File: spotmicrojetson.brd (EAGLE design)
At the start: 31 x 66 mm, 6 parts, among them J1 I2C1, J2 I2C2, J3 I2C3, J4 I2C4

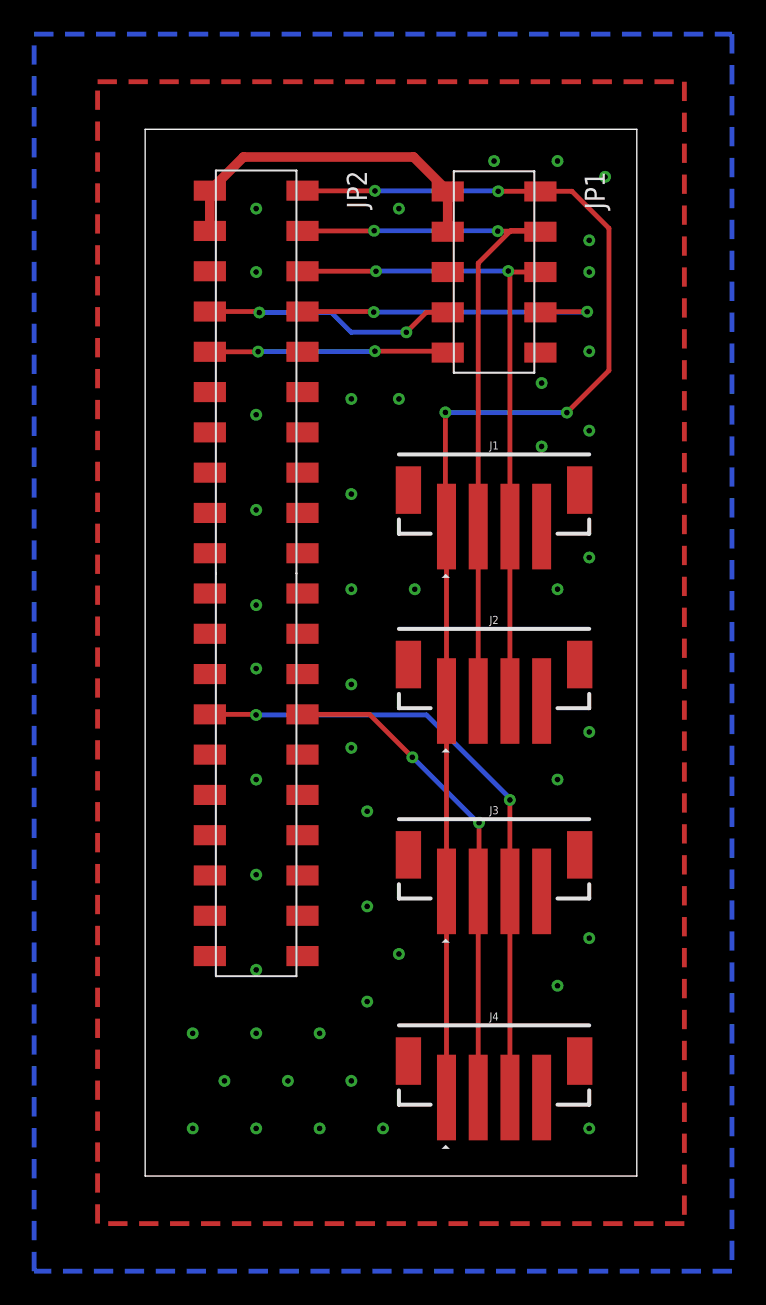
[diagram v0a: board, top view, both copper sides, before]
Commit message: Fix ground plane polygons
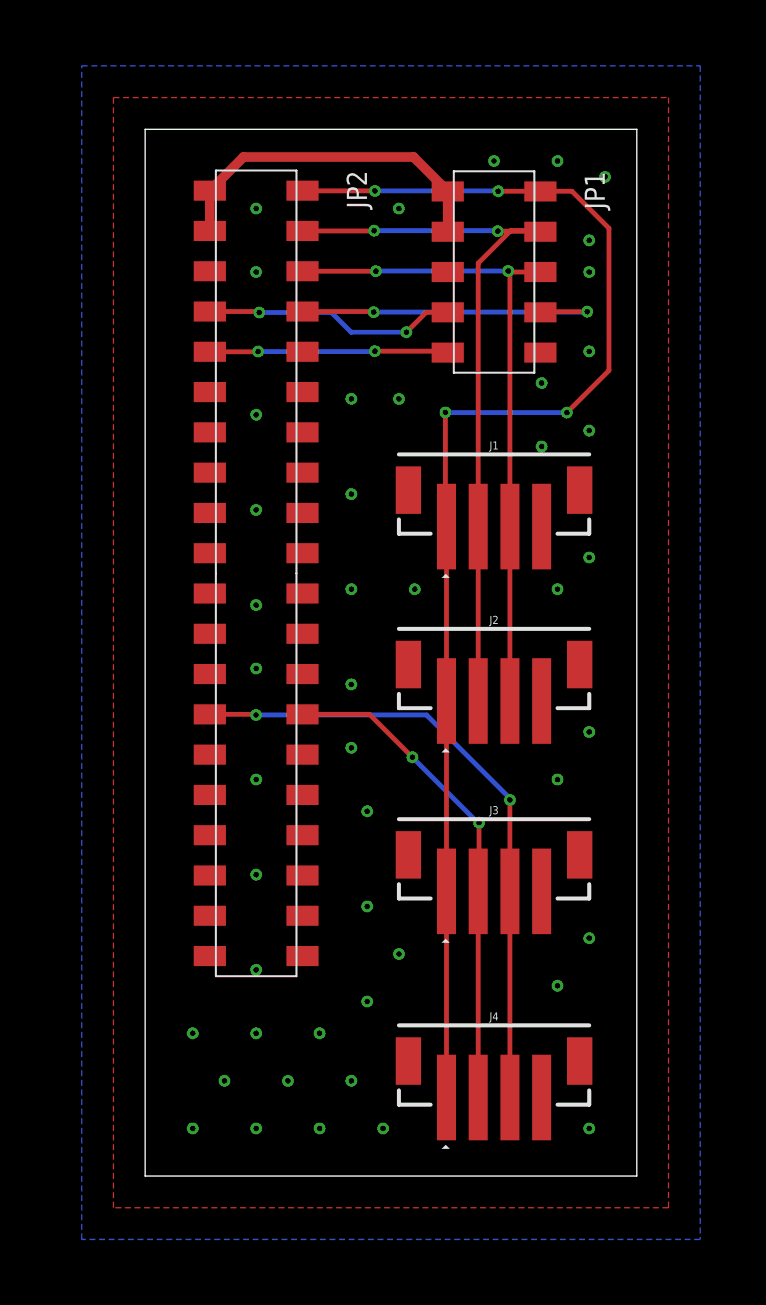
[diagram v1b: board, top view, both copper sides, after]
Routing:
- net N$2: track 244.0 -> 0.00 mm
- net N$1: track 218.0 -> 0.00 mm
- added copper zone on layer 1, net GND
- added copper zone on layer 16, net GND
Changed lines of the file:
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@@
 <via x="52" y="84" extent="1-16" drill="0.35"/>
 <via x="54" y="23" extent="1-16" drill="0.35"/>
+<polygon width="0.3048" layer="1">
+<vertex x="24" y="88"/>
+<vertex x="59" y="88"/>
+<vertex x="59" y="18"/>
+<vertex x="24" y="18"/>
+</polygon>
+<polygon width="0.3048" layer="16">
+<vertex x="22" y="90"/>
+<vertex x="61" y="90"/>
+<vertex x="61" y="16"/>
+<vertex x="22" y="16"/>
+</polygon>
 <wire x1="52" y1="84" x2="55" y2="83" width="0" layer="19" extent="1-1"/>
 <wire x1="48" y1="84" x2="52" y2="84" width="0" layer="19" extent="1-1"/>
@@
 <wire x1="44.99" y1="72.009" x2="45.079" y2="71.92" width="0.3048" layer="1"/>
 </signal>
-<signal name="N$1">
-<wire x1="23" y1="89" x2="60" y2="89" width="0.3048" layer="1" style="longdash"/>
-<wire x1="60" y1="89" x2="60" y2="17" width="0.3048" layer="1" style="longdash"/>
-<wire x1="60" y1="17" x2="23" y2="17" width="0.3048" layer="1" style="longdash"/>
-<wire x1="23" y1="17" x2="23" y2="89" width="0.3048" layer="1" style="longdash"/>
-</signal>
-<signal name="N$2">
-<wire x1="19" y1="92" x2="63" y2="92" width="0.3048" layer="16" style="longdash"/>
-<wire x1="63" y1="92" x2="63" y2="14" width="0.3048" layer="16" style="longdash"/>
-<wire x1="63" y1="14" x2="19" y2="14" width="0.3048" layer="16" style="longdash"/>
-<wire x1="19" y1="14" x2="19" y2="92" width="0.3048" layer="16" style="longdash"/>
-</signal>
 </signals>

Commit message: Optimize layout
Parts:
- moved J4 3.00 mm to (48.0, 29.0)
- moved J3 1.00 mm to (48.0, 40.0)
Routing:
- net VDD: track 84.2 -> 81.2 mm
- net SDA2: track 31.7 -> 30.2 mm
- net SCL2: track 40.6 -> 39.1 mm
- net GND: vias 47 -> 43
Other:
- board size 31 x 66 mm -> 31 x 63 mm
